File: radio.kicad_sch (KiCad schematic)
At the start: 24 parts, among them IC5 S2-LPQTR, IC6 BALF-SPI2-01D3, Y3 NX1612SA-50M-EXS00A-CS08403

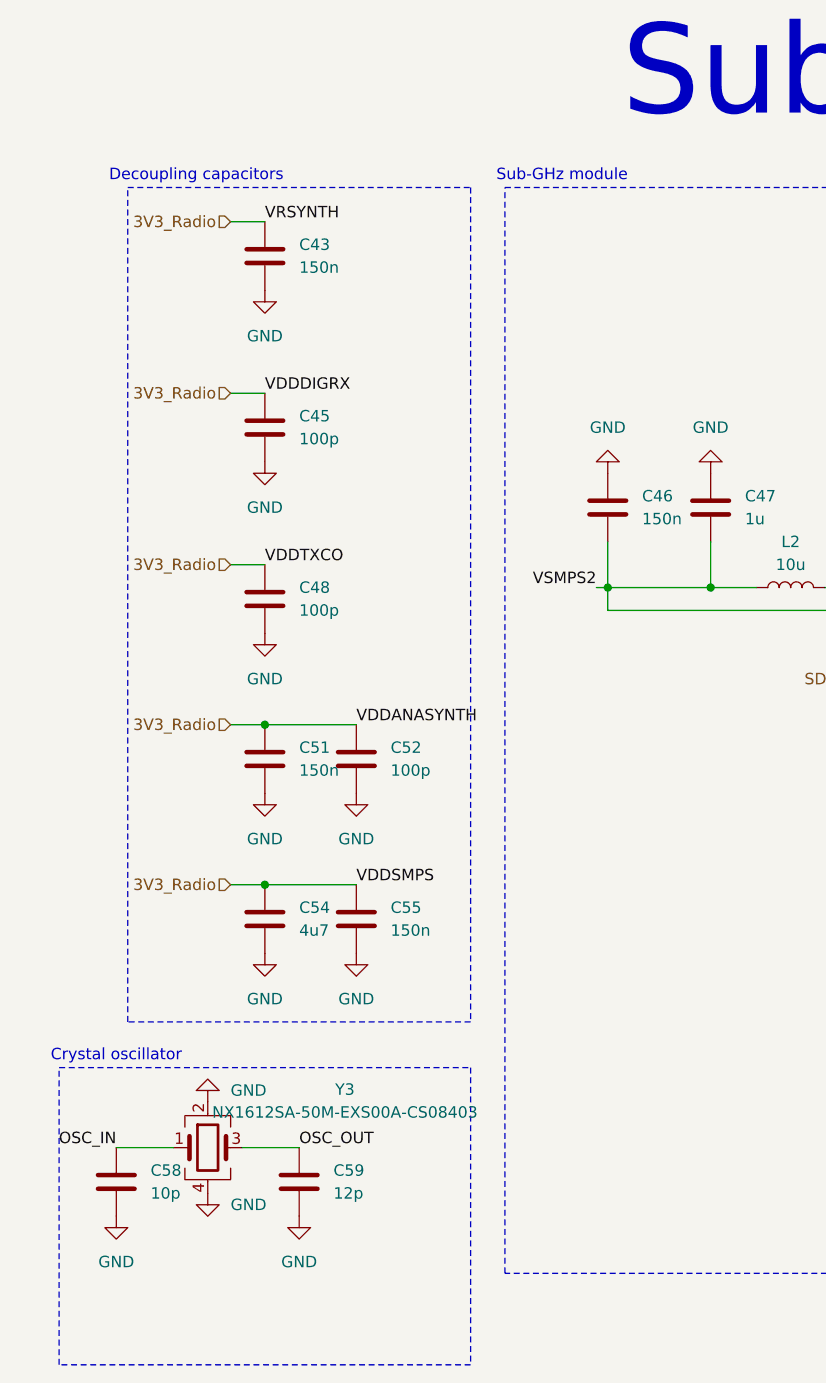
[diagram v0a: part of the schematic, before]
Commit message: Update schematic to Kicad 10
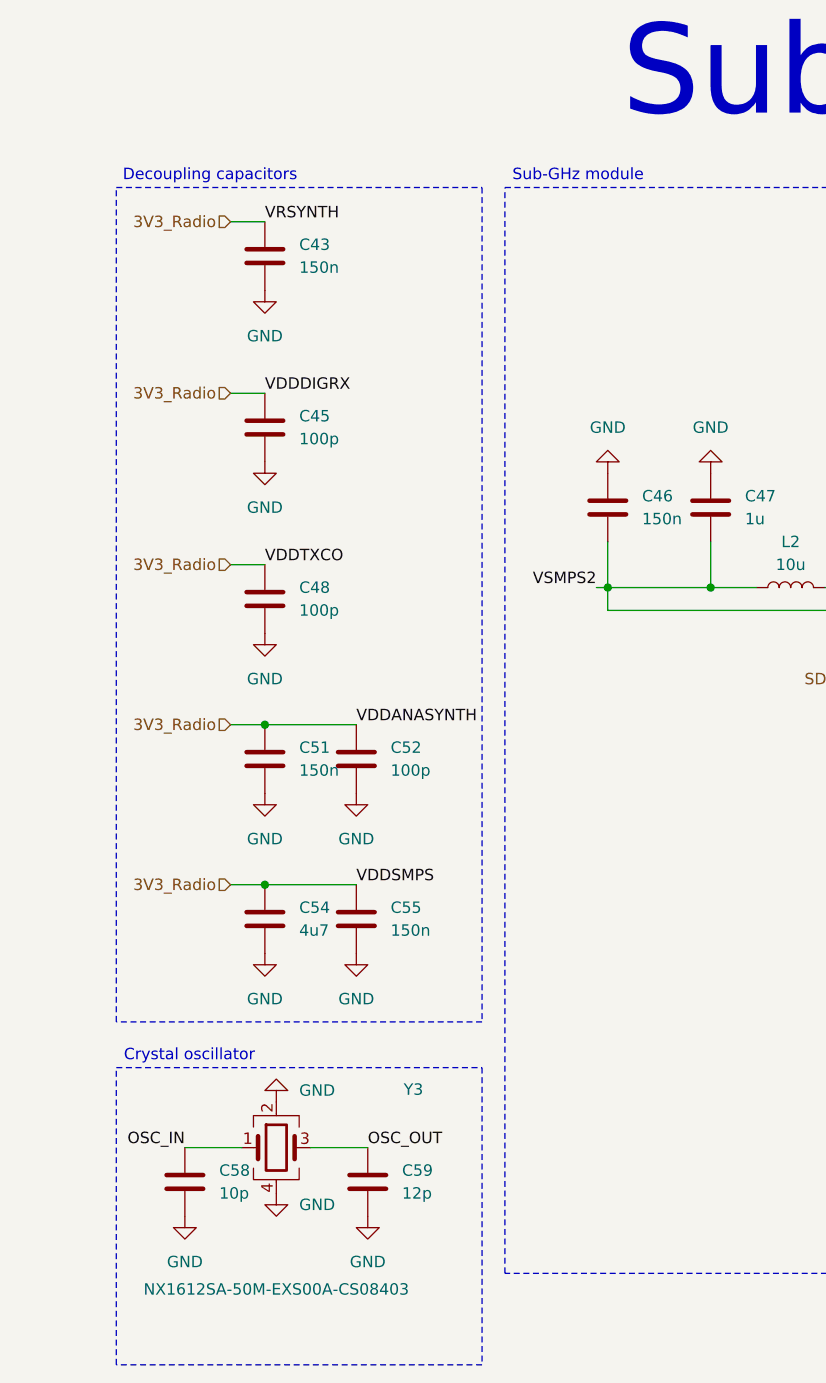
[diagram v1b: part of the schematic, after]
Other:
- moved on the sheet: C58, C59, Y3

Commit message: Add tests points with 5015 footprint for practicity
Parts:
- renumbered C58 to C43, C43 to C44, C48 to C46, C51 to C47, C54 to C48, C52 to C49, C55 to C50, C59 to C51, C46 to C52, C47 to C53, C57 to C54, C44 to C55, C53 to C56, C56 to C57, C49 to C58, C50 to C59
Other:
- moved on the sheet: C43, C44, C45, C46, C47, C48, C49, C50, C51, Y3

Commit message: Do no mount antenna coaxial antenna, to be soldered after by hand
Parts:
- AE1: now not fitted
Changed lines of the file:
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@@
 		(on_board yes)
 		(in_pos_files yes)
-		(dnp no)
+		(dnp yes)
 		(fields_autoplaced yes)
 		(property "Reference" "AE1"

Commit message: Add pull ups resistors for I2C bus and reformat some schematic files
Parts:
- renumbered R7 to R11
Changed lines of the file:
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@@
 		(in_pos_files yes)
 		(dnp no)
-		(property "Reference" "R7"
+		(property "Reference" "R11"
 			(at 142.24 124.46 90)
 			(show_name no)
@@
 			(project "weather-station-poc"
 				(path "/38eb53bb-294e-46e4-ad59-fd355ca373b9/31741ecc-719f-4191-b75e-d75152dfd251"
-					(reference "R7")
+					(reference "R11")
 					(unit 1)
 				)

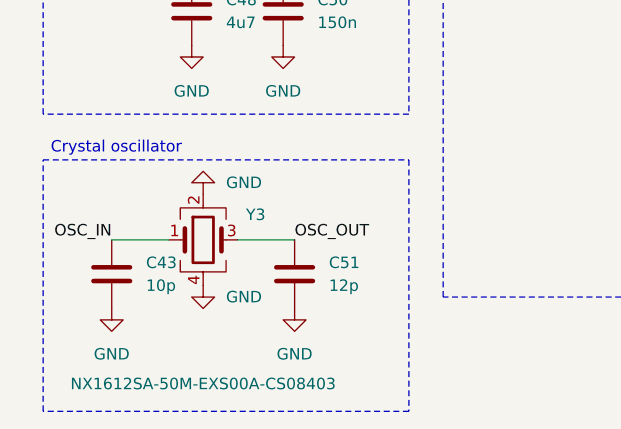
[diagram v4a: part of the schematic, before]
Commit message: Complete all references for components
Modifgy Y1 and Y2 capacitors footprint from 0603 to 0402
Modify footprint of SWD connector
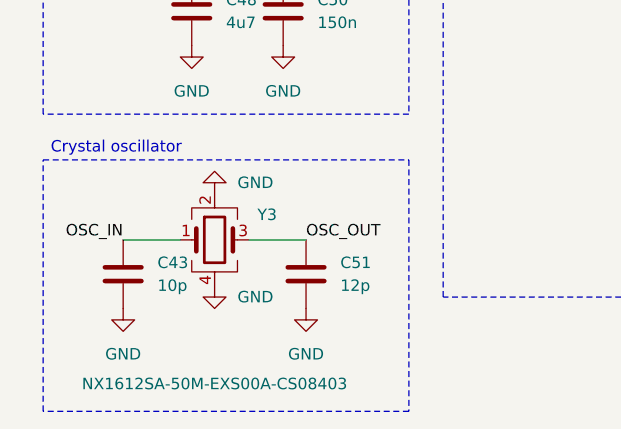
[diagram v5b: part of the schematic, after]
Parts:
- AE1: Manufacturer_Name (none) -> Molex; Manufacturer_Part_Number (none) -> 73251-1153
- C43: Manufacturer_Name (none) -> Wurth Elektronik; Manufacturer_Part_Number (none) -> 885012006002
- C44, C47, C50, C52, C55, C56, C57: Manufacturer_Name (none) -> Wurth Elektronik; Manufacturer_Part_Number (none) -> 885012206021
- C45, C46, C49, C58: Manufacturer_Name (none) -> Wurth Elektronik; Manufacturer_Part_Number (none) -> 885012206003
- C48: Manufacturer_Name (none) -> Murata Electronics; Manufacturer_Part_Number (none) -> GRM188Z71A475KE15J
- C51: Manufacturer_Name (none) -> Vishay; Manufacturer_Part_Number (none) -> VJ0603A120FXQCW1BC
- C53: Manufacturer_Name (none) -> Wurth Elektronik; Manufacturer_Part_Number (none) -> 885012206026
- C54: Manufacturer_Name (none) -> Wurth Elektronik; Manufacturer_Part_Number (none) -> 885012206006
- C59: Manufacturer_Name (none) -> Vishay; Manufacturer_Part_Number (none) -> VJ0603A2R7BXQCW1BC
- L2: Manufacturer_Name (none) -> Murata Electronics; Manufacturer_Part_Number (none) -> LQM21FN100M80L
- L3: Manufacturer_Name (none) -> Murata Electronics; Manufacturer_Part_Number (none) -> LQW18AN12NG00D
- R11: Manufacturer_Name (none) -> Wurth Elektronik; Manufacturer_Part_Number (none) -> 560050316012
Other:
- moved on the sheet: C43, C51, Y3
